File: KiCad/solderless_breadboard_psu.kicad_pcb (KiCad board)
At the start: 2 copper layers, 86 parts, among them IC301 MCP73831T-2ACI_OT, IC302 BQ29737DSER, IC401 TLV62569DBVR, IC501 FT232RL-REEL, J201 Barrel_Jack_Switch_Pin3Ring, J301 BM02B-GHS-TBT_LF__SN__N_, J501 Conn_01x09_Pin, J502 Conn_01x09_Pin, J503 Conn_01x06_Pin, J504 USB_C_Receptacle_USB2.0, J601 Conn_02x03_Odd_Even, J602 Conn_02x03_Odd_Even, Q301 DMG3415U-7, Q302 T2N7002AK, Q303 T2N7002AK, U401 TPS61040DBVR, U501 USBLC6-2SC6

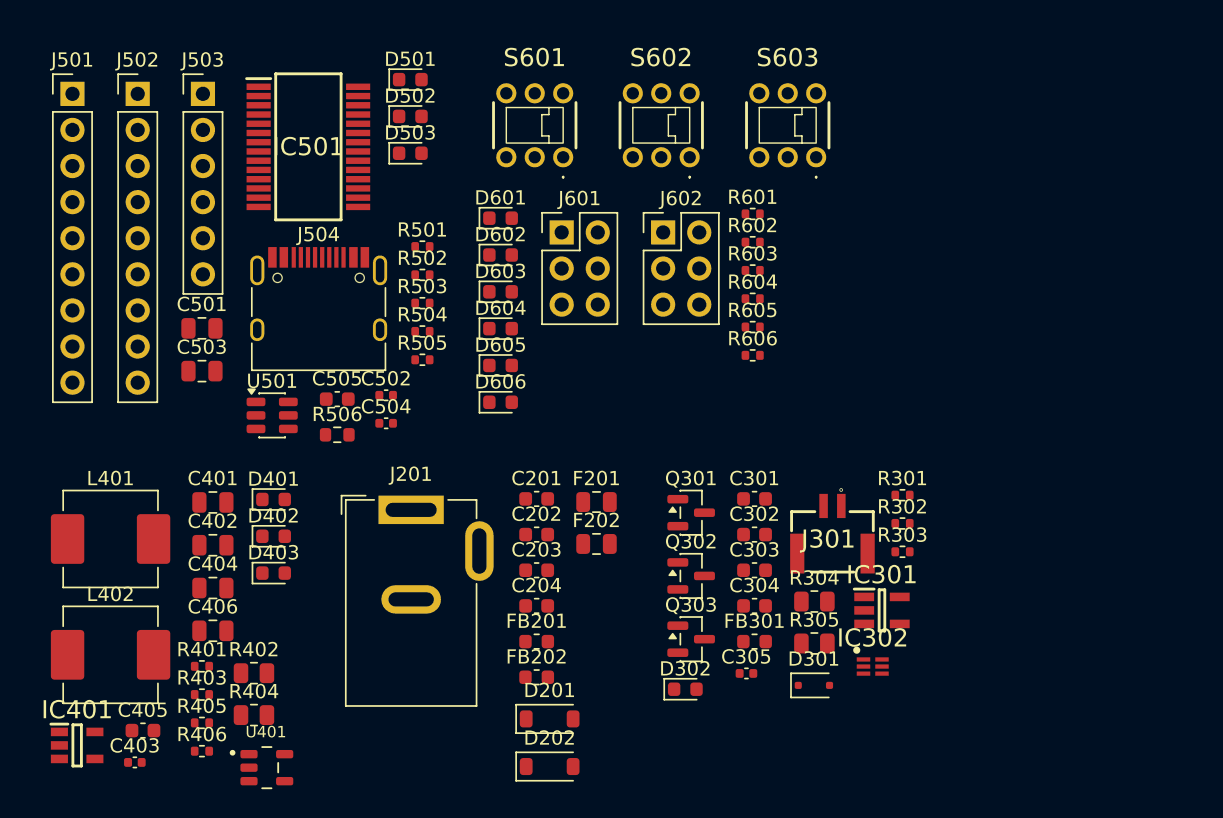
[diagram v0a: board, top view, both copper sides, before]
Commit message: ERC fixes
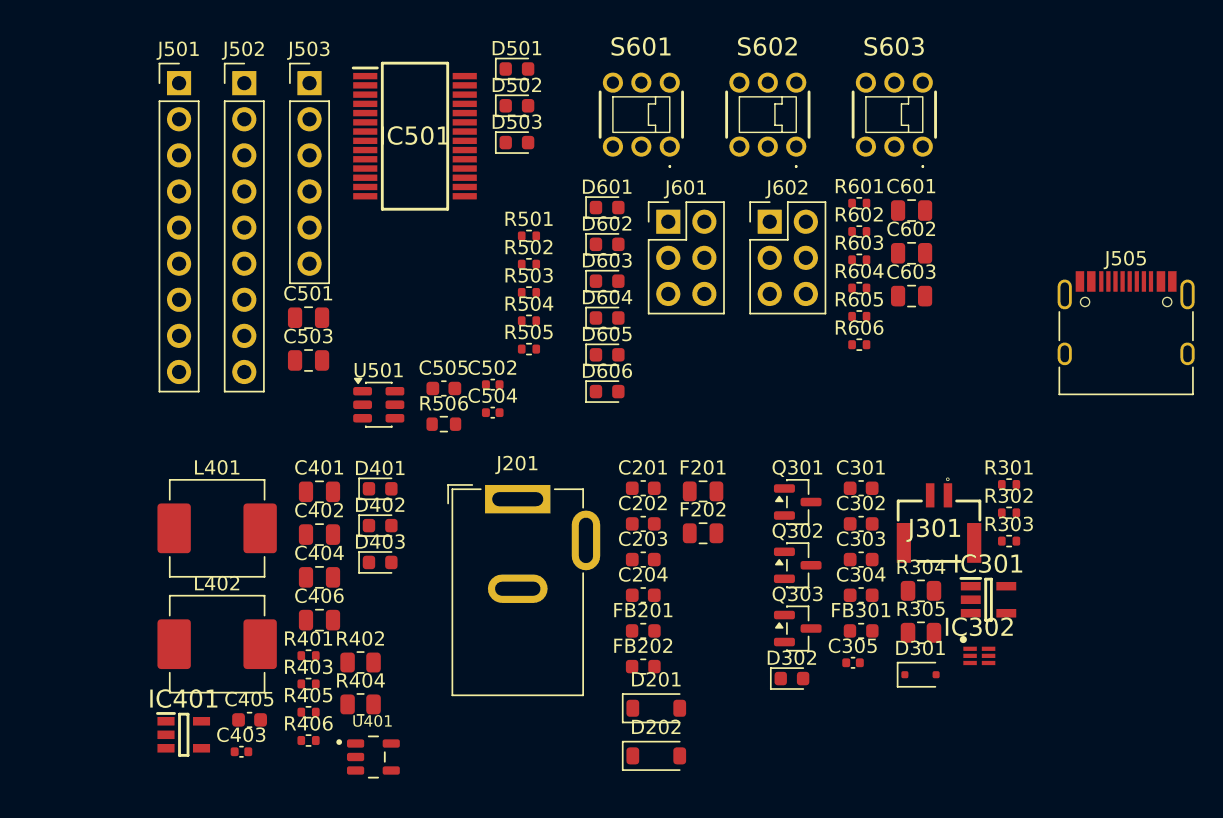
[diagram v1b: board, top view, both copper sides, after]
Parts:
- removed J504: USB_C_Receptacle_USB2.0, Connector_USB:USB_C_Receptacle_HRO_TYPE-C-31-M-12
- added C601: 22uF, Capacitor_SMD:C_0805_2012Metric, F.Cu at (105.3, 38.7)
- added C602: 22uF, Capacitor_SMD:C_0805_2012Metric, F.Cu at (105.3, 41.7)
- added C603: 22uF, Capacitor_SMD:C_0805_2012Metric, F.Cu at (105.3, 44.7)
- added J505: USB_C_Receptacle_USB2.0_16P, Connector_USB:USB_C_Receptacle_HRO_TYPE-C-31-M-12, F.Cu at (120.4, 47.7)
- moved C201 7.54 mm to (86.5, 58.2)
- moved C202 7.54 mm to (86.5, 60.7)
- moved C203 7.54 mm to (86.5, 63.2)
- moved C204 7.54 mm to (86.5, 65.7)
- moved C301 7.54 mm to (101.8, 58.2)
- moved C302 7.54 mm to (101.8, 60.7)
- moved C303 7.54 mm to (101.8, 63.2)
- moved C304 7.54 mm to (101.8, 65.7)
- moved C305 7.54 mm to (101.2, 70.5)
- moved C401 7.54 mm to (63.7, 58.5)
- moved C402 7.54 mm to (63.7, 61.5)
- moved C403 7.54 mm to (58.2, 76.7)
- moved C404 7.54 mm to (63.7, 64.5)
- moved C405 7.54 mm to (58.8, 74.5)
- moved C406 7.54 mm to (63.7, 67.5)
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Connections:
- D601 pad 1: Net-(D601-K) -> GND
- D602 pad 1: Net-(D602-K) -> GND
- D603 pad 1: Net-(D603-K) -> GND
- D604 pad 1: Net-(D604-K) -> GND
- D605 pad 1: Net-(D605-K) -> GND
- D606 pad 1: Net-(D606-K) -> GND
- J501 pad 8: /[5]USB 2 UART/DCD -> /[5]USB 2 UART/DSR
- J503 pad 4: FTDI_VCC -> VCC_FTDI
- R601 pad 2: +VIN_SWITCH -> Net-(R601-Pad2)
- R602 pad 2: +VIN_SWITCH -> Net-(R602-Pad2)
- R603 pad 2: +VIN_SWITCH -> Net-(R603-Pad2)
- R604 pad 2: +VIN_SWITCH -> Net-(R604-Pad2)
- R605 pad 2: +VCC_USB2UART_FILT -> Net-(R605-Pad2)
- R606 pad 2: +VCC_USB2UART_FILT -> Net-(R606-Pad2)
- S601 pad 4: Net-(D601-K) -> Net-(R601-Pad2)
- S601 pad 5: GND -> +VIN_SWITCH
- S601 pad 6: Net-(D602-K) -> Net-(R602-Pad2)
- S602 pad 4: Net-(D603-K) -> Net-(R603-Pad2)
- S602 pad 5: GND -> +VIN_SWITCH
- S602 pad 6: Net-(D604-K) -> Net-(R604-Pad2)
- S603 pad 4: Net-(D605-K) -> Net-(R605-Pad2)
- S603 pad 5: GND -> +VCC_USB2UART_FILT
- S603 pad 6: Net-(D606-K) -> Net-(R606-Pad2)

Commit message: basic PCB
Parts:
- moved D501 104.3 mm to (150.0, 103.8), turned to 180 degrees
- moved C505 104.2 mm to (146.2, 124.8), turned to -90 degrees
- moved D502 103.9 mm to (150.0, 105.8), turned to 180 degrees
- moved C501 103.7 mm to (146.5, 107.5)
- moved D503 103.5 mm to (150.0, 107.8), turned to 180 degrees
- moved C503 103.3 mm to (146.4, 110.0)
- moved R502 101.8 mm to (146.0, 118.5), turned to 90 degrees
- moved R506 100.1 mm to (146.2, 121.3), turned to 90 degrees
- moved IC501 100.0 mm to (139.5, 105.8)
- moved R503 95.8 mm to (146.5, 111.8), turned to 180 degrees
- moved R501 95.4 mm to (133.2, 118.5), turned to 90 degrees
- moved U501 94.7 mm to (139.5, 114.3), turned to 90 degrees
- moved R504 89.1 mm to (146.0, 104.5)
- moved R505 88.7 mm to (146.0, 105.8)
- moved C303 87.2 mm to (171.5, 115.5)
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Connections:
- J502 pad 9: /[5]USB 2 UART/DTR -> /[5]USB 2 UART/RX_LED

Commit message: minor pcb update
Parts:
- moved R405 201.6 mm to (264.4, 80.3)
- moved R406 201.6 mm to (264.4, 82.3)
- moved D402 201.6 mm to (269.5, 67.2)
- moved D403 201.6 mm to (269.5, 69.8)
- moved C403 178.9 mm to (237.0, 83.8)
- moved IC401 178.9 mm to (232.9, 82.6)
- moved L402 178.9 mm to (235.2, 76.2)
- moved R401 178.9 mm to (241.7, 77.0)
- moved R403 178.9 mm to (241.7, 79.0)
- moved C401 178.9 mm to (242.4, 65.5)
- moved C402 178.9 mm to (242.4, 68.5)
- moved C405 139.8 mm to (198.5, 77.5)
- moved D401 139.8 mm to (207.7, 61.2)
- moved L401 139.8 mm to (196.2, 64.0)
- moved R402 139.8 mm to (206.3, 73.5)
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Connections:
- net Net-(IC302-BAT) renamed /[3] Battery/BAT
- net Net-(IC302-COUT) renamed /[3] Battery/COUT
- net Net-(IC302-DOUT) renamed /[3] Battery/DOUT
- net Net-(IC302-V-) renamed /[3] Battery/V-
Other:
- copper layers 2 -> 4

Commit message: Calculated pin headers positions
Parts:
- removed D503: LED, LED_SMD:LED_0603_1608Metric
- removed J505: USB_C_Receptacle_USB2.0_16P, Connector_USB:USB_C_Receptacle_HRO_TYPE-C-31-M-12
- removed R506: DNP, 1MR, Resistor_SMD:R_0603_1608Metric
- added J504: USB_C_Receptacle_USB2.0_16P, Connector_USB:USB_C_Receptacle_HRO_TYPE-C-31-M-12, F.Cu at (51.5, 98.8)
- R505: value 510R -> DNP, 1MR; footprint Resistor_SMD:R_0402_1005Metric -> Resistor_SMD:R_0603_1608Metric
- moved D402 221.0 mm to (48.8, 79.8)
- moved D403 217.4 mm to (52.3, 79.8), turned to 180 degrees
- moved R405 215.6 mm to (48.8, 81.5)
- moved R406 212.1 mm to (52.3, 81.2)
- moved D401 187.8 mm to (22.2, 90.5)
- moved R402 185.5 mm to (22.1, 94.8)
- moved C406 182.8 mm to (22.0, 92.5)
- moved R404 181.4 mm to (25.8, 94.8)
- moved U401 181.1 mm to (26.5, 91.5)
- moved C405 177.5 mm to (22.1, 96.8)
- moved C404 175.1 mm to (30.0, 91.5), turned to -90 degrees
- moved C401 174.1 mm to (70.2, 91.2), turned to -90 degrees
- moved L401 171.6 mm to (26.0, 85.8), turned to 180 degrees
- moved R403 170.8 mm to (71.5, 94.0)
- moved R401 168.8 mm to (73.8, 94.0)
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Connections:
- R503 pad 1: Net-(D503-A) -> /[5]USB 2 UART/RX_LED
- R503 pad 2: +3V3_FTDI -> Net-(D501-K)
- R504 pad 1: /[5]USB 2 UART/RX_LED -> /[5]USB 2 UART/TX_LED
- R504 pad 2: Net-(D501-K) -> Net-(D502-K)
- R505 pad 1: /[5]USB 2 UART/TX_LED -> GNDPWR
- R505 pad 2: Net-(D502-K) -> GND

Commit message: minor PCB updates
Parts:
- moved C201 28.4 mm to (32.5, 110.8)
- moved C203 28.4 mm to (37.3, 110.7)
- moved C204 28.4 mm to (37.2, 108.5)
- moved D201 28.4 mm to (31.6, 106.2)
- moved D202 28.4 mm to (38.0, 106.2)
- moved F201 28.4 mm to (32.3, 113.2)
- moved F202 28.4 mm to (38.5, 113.2)
- moved FB201 28.4 mm to (29.5, 109.5)
- moved FB202 28.4 mm to (40.0, 109.5)
- moved C202 28.4 mm to (32.5, 108.5)
- moved C404 15.4 mm to (43.7, 84.5)
- moved C405 15.4 mm to (35.8, 89.8)
- moved C406 15.4 mm to (35.7, 85.5)
- moved D401 15.4 mm to (36.0, 83.5)
- moved L401 15.4 mm to (39.7, 78.8)
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
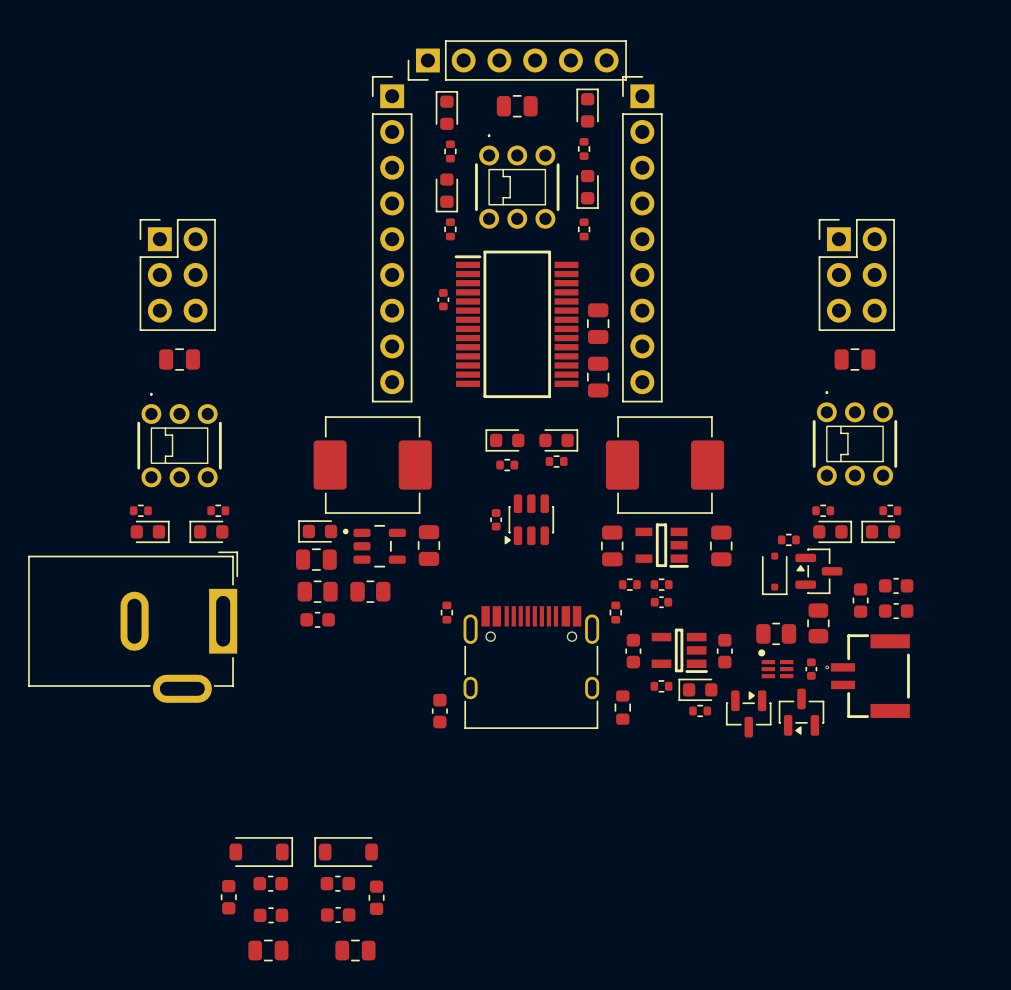
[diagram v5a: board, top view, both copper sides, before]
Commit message: Add board edge cuts
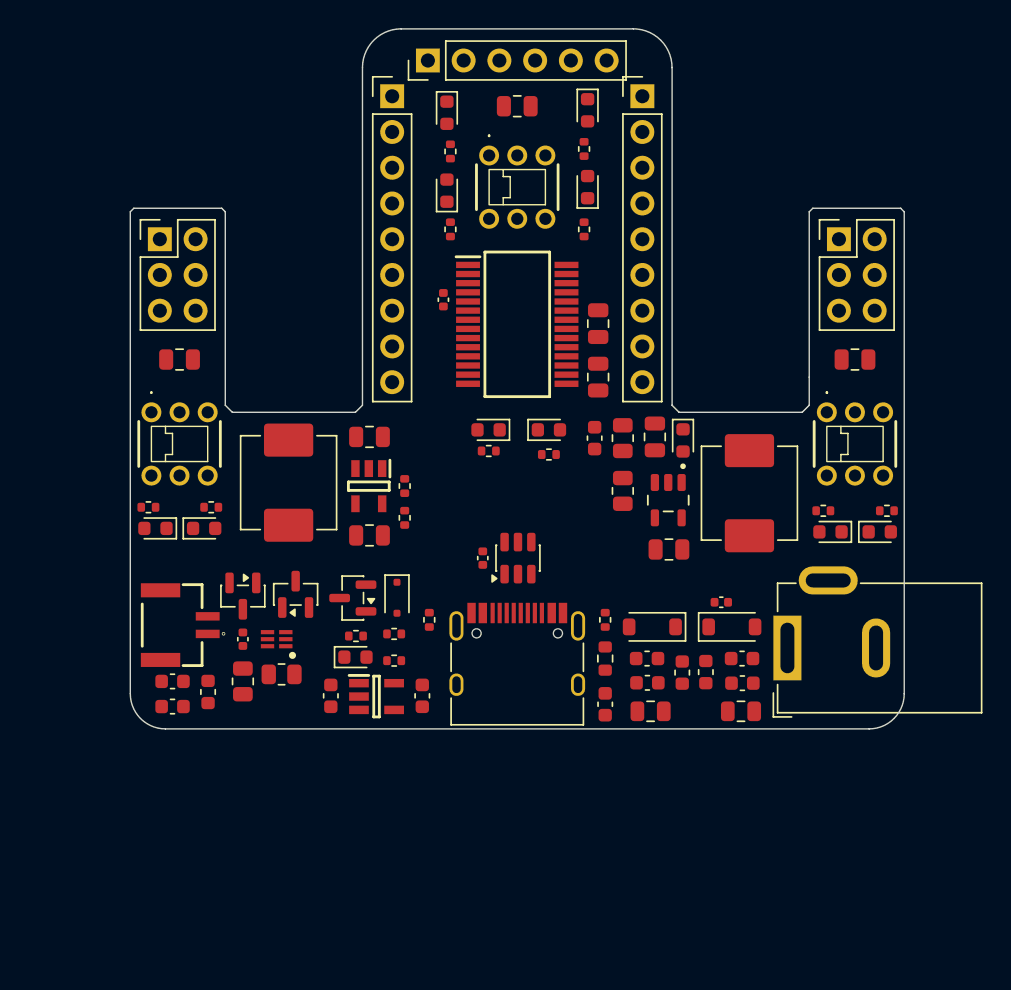
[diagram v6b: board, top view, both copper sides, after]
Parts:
- moved C304 52.1 mm to (25.5, 95.9), turned to 180 degrees
- moved C303 51.7 mm to (25.5, 94.1), turned to 180 degrees
- moved FB301 46.8 mm to (28.0, 94.9), turned to -90 degrees
- moved J301 45.3 mm to (28.0, 90.1), turned to -90 degrees
- moved R304 41.1 mm to (30.5, 94.1), turned to 90 degrees
- moved Q303 40.5 mm to (30.5, 88.1), turned to -90 degrees
- moved C305 40.5 mm to (30.5, 91.1), turned to 90 degrees
- moved J201 40.1 mm to (69.2, 91.8), turned to 90 degrees
- moved F201 37.6 mm to (65.9, 96.2), turned to 180 degrees
- moved FB201 37.5 mm to (63.4, 93.5)
- moved C201 37.3 mm to (66.0, 94.2)
- moved D201 37.2 mm to (65.2, 90.2), turned to 0 degrees
- moved C202 37.1 mm to (66.0, 92.5)
- moved IC302 35.7 mm to (32.9, 91.1), turned to 180 degrees
- moved R305 35.3 mm to (33.3, 93.6), turned to 0 degrees
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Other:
- board outline added: 55 x 49.8 mm

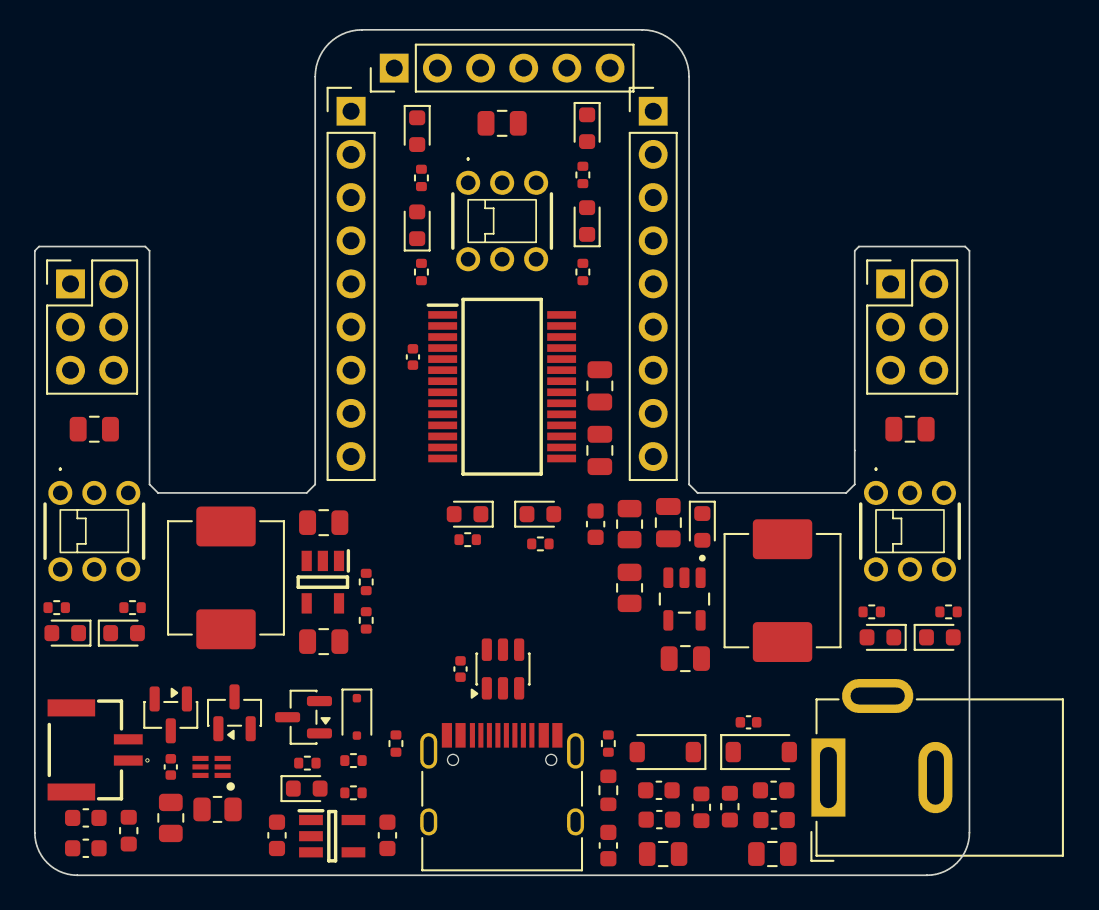
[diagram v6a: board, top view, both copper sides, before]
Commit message: Update FTDI pin header
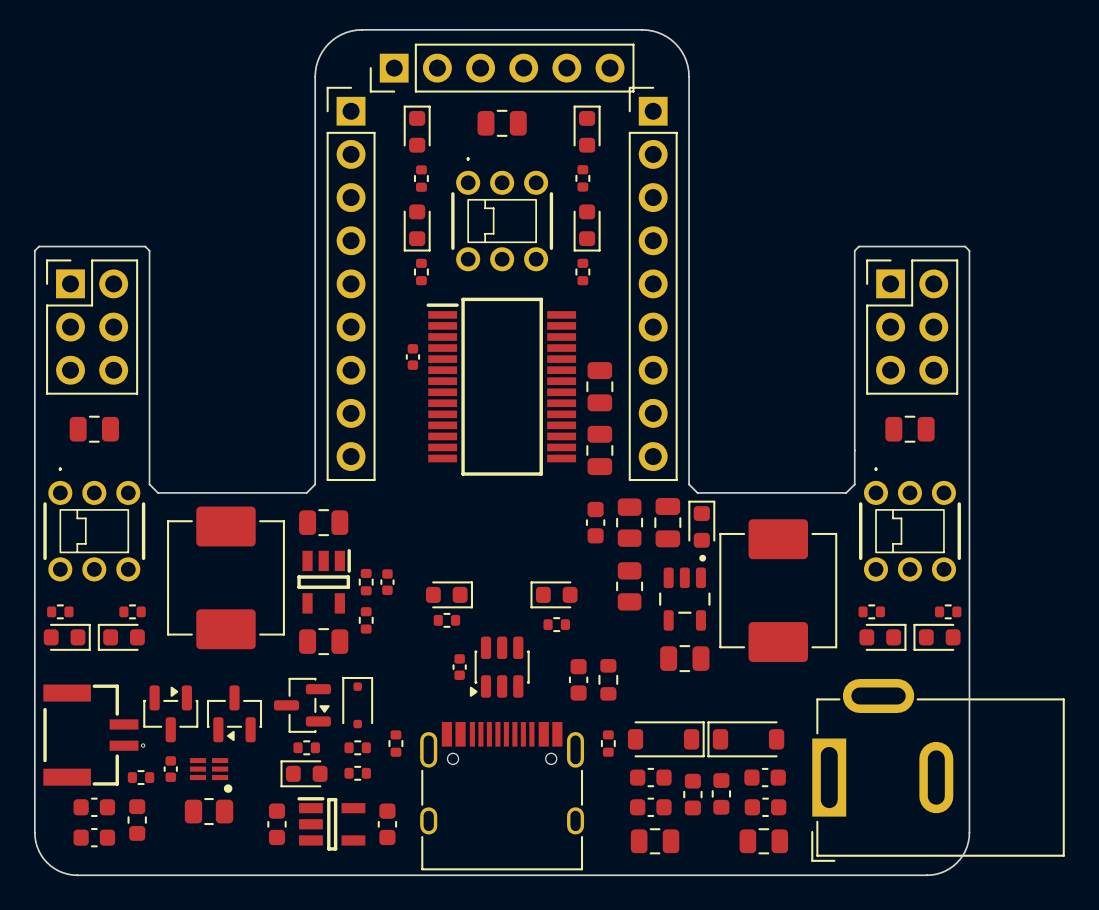
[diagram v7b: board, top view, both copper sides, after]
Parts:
- R304: footprint Resistor_SMD:R_0805_2012Metric -> Resistor_SMD:R_0402_1005Metric
- moved C403 22.8 mm to (43.2, 80.2), turned to -90 degrees
- moved C505 9.91 mm to (54.5, 86.0), turned to 90 degrees
- moved R505 6.50 mm to (56.2, 86.0)
- moved D403 4.90 mm to (46.7, 81.0)
- moved R406 4.90 mm to (46.8, 82.5)
- moved D402 4.85 mm to (53.2, 81.0)
- moved R405 4.85 mm to (53.2, 82.8)
- moved R304 2.95 mm to (28.8, 91.8), turned to 0 degrees
- moved R303 1.18 mm to (41.5, 91.5)
- moved D201 1.06 mm to (64.5, 89.5)
- moved J301 0.91 mm to (27.8, 89.2)
- moved C201 0.90 mm to (65.5, 93.5)
- moved C202 0.90 mm to (65.5, 91.8)
- moved F201 0.90 mm to (65.4, 95.5)
- moved FB201 0.90 mm to (62.9, 92.7)
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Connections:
- J502 pad 1: /[5]USB 2 UART/PWREN -> /[5]USB 2 UART/RX_LED
- J502 pad 2: /[5]USB 2 UART/TEN -> GND
- J502 pad 3: /[5]USB 2 UART/SLEEP -> /[5]USB 2 UART/TX_LED
- J502 pad 4: /[5]USB 2 UART/CTS -> +VCC_USB2UART_FILT
- J502 pad 6: +VCC_USB2UART_FILT -> /[5]USB 2 UART/CTS
- J502 pad 7: /[5]USB 2 UART/TX_LED -> /[5]USB 2 UART/SLEEP
- J502 pad 8: GND -> /[5]USB 2 UART/TEN
- J502 pad 9: /[5]USB 2 UART/RX_LED -> /[5]USB 2 UART/PWREN
